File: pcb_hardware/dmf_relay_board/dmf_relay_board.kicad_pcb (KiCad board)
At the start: 2 copper layers, 100 x 96.5 mm, 64 parts, among them J1 HVPS, J2 Relays to Electrodes 1, J3 Relays to Electrodes 2, J4 Electrodes from Relay 1, J5 Electrodes from Relay 2, U1 HV507

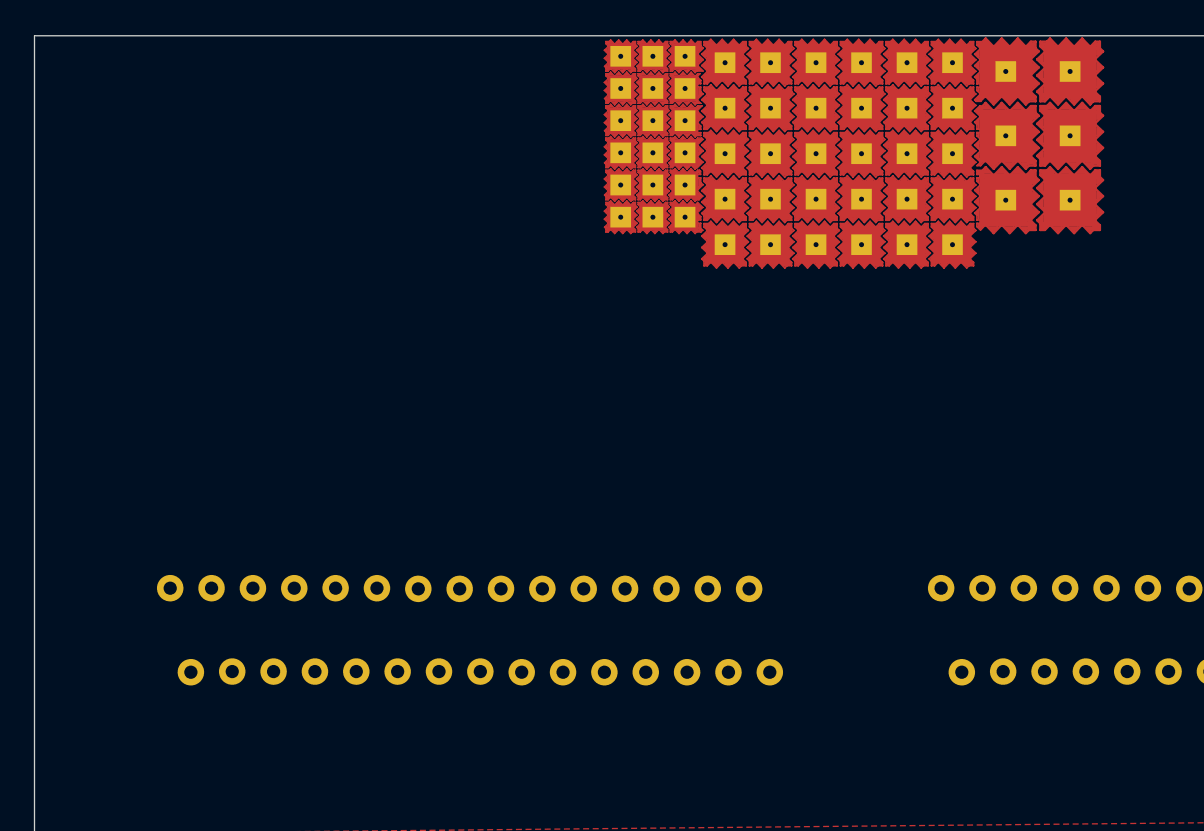
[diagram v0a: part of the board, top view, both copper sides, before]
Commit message: electrode configuration changed for routing management
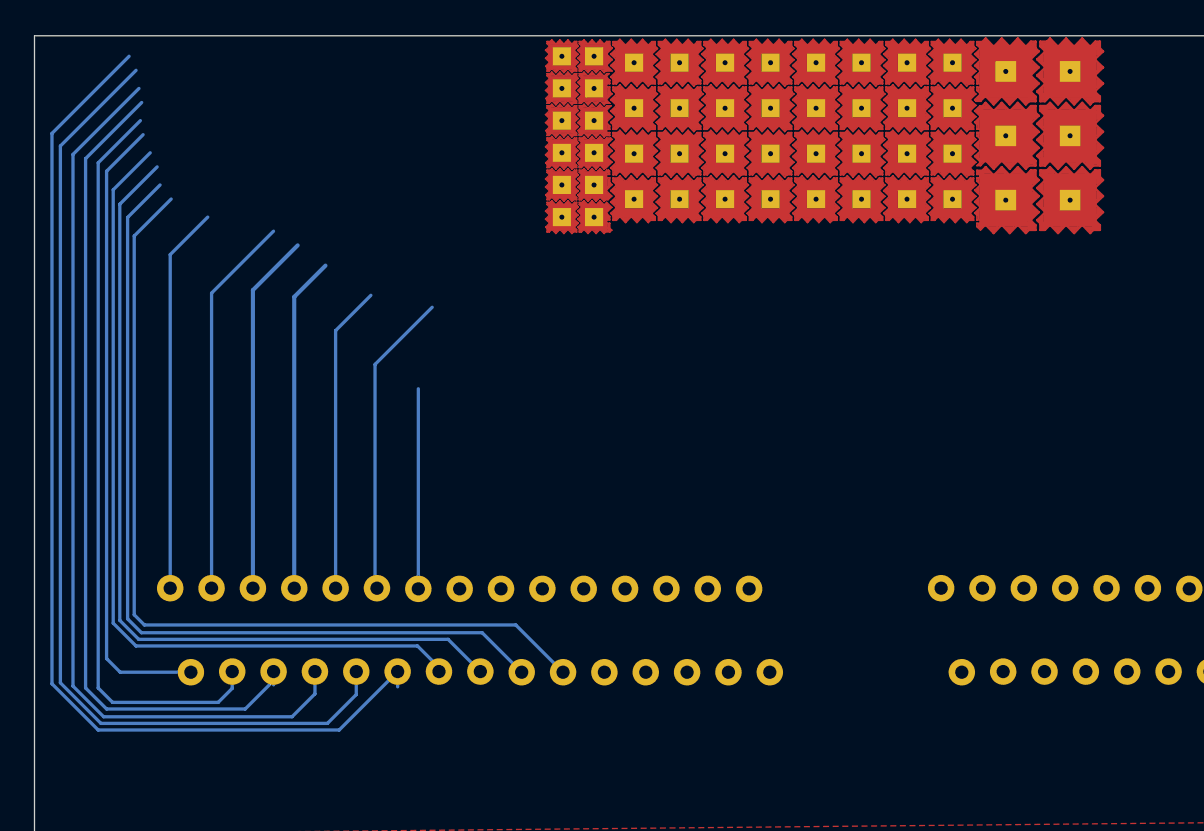
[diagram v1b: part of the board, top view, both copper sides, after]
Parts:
- removed EXS13, EXS14, EXS16, EXS17: ELEC_XS, dmf_relay_board:ELECTRODE_1_375_4MIL_4_5
- removed EXS15: ELEC_XS_TO_SM_5, dmf_relay_board:ELEC_XS_TO_SM_NUM5
- removed EXS18: ELEC_XS_TO_SM_6, dmf_relay_board:ELEC_XS_TO_SM_NUM6
- added ESM31: ELEC_SML, dmf_relay_board:ELECTRODE_2_75_4MIL_4_5, F.Cu at (164.7, 63.9)
- added ESM32: ELEC_SML, dmf_relay_board:ELECTRODE_2_75_4MIL_4_5, F.Cu at (167.5, 63.9)
- EXS10: value ELEC_XS -> ELEC_XS_TO_SM_5; footprint dmf_relay_board:ELECTRODE_1_375_4MIL_4_5 -> dmf_relay_board:ELEC_XS_TO_SM_NUM5
- EXS12: value ELEC_XS_TO_SM_4 -> ELEC_XS_TO_SM_6; footprint dmf_relay_board:ELEC_XS_TO_SM_NUM4 -> dmf_relay_board:ELEC_XS_TO_SM_NUM6
- EXS2: value ELEC_XS -> ELEC_XS_TO_SM_1; footprint dmf_relay_board:ELECTRODE_1_375_4MIL_4_5 -> dmf_relay_board:ELEC_XS_TO_SM_NUM1
- EXS3: value ELEC_XS_TO_SM_1 -> ELEC_XS; footprint dmf_relay_board:ELEC_XS_TO_SM_NUM1 -> dmf_relay_board:ELECTRODE_1_375_4MIL_4_5
- EXS4: value ELEC_XS -> ELEC_XS_TO_SM_2; footprint dmf_relay_board:ELECTRODE_1_375_4MIL_4_5 -> dmf_relay_board:ELEC_XS_TO_SM_NUM2
- EXS6: value ELEC_XS_TO_SM_2 -> ELEC_XS_TO_SM_3; footprint dmf_relay_board:ELEC_XS_TO_SM_NUM2 -> dmf_relay_board:ELEC_XS_TO_SM_NUM3
- EXS8: value ELEC_XS -> ELEC_XS_TO_SM_4; footprint dmf_relay_board:ELECTRODE_1_375_4MIL_4_5 -> dmf_relay_board:ELEC_XS_TO_SM_NUM4
- EXS9: value ELEC_XS_TO_SM_3 -> ELEC_XS; footprint dmf_relay_board:ELEC_XS_TO_SM_NUM3 -> dmf_relay_board:ELECTRODE_1_375_4MIL_4_5
- moved ESM17 16.5 mm to (148.2, 61.2)
- moved ESM18 16.5 mm to (151.0, 61.2)
- moved ESM7 11.3 mm to (164.7, 55.7)
- moved ESM8 11.3 mm to (167.5, 55.7)
- moved ESM10 11.0 mm to (151.0, 58.4)
- moved ESM11 11.0 mm to (153.7, 58.4)
- moved ESM12 11.0 mm to (156.5, 58.4)
- moved ESM9 11.0 mm to (148.2, 58.4)
- moved EXS9 8.40 mm to (143.9, 63.1)
- moved EXS3 7.70 mm to (143.9, 57.2)
- moved EXS11 6.74 mm to (143.9, 65.0)
- moved EXS12 6.74 mm to (145.8, 65.0)
- moved ESM13 6.15 mm to (159.2, 58.4)
- moved ESM14 6.15 mm to (162.0, 58.4)
- moved ESM15 6.15 mm to (164.7, 58.4)
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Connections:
- J4 pad 1: Net-(EXS1-Pad1) -> Net-(J4-Pad1)
- J4 pad 10: Net-(EXS8-Pad1) -> Net-(J4-Pad10)
- J4 pad 11: Net-(EXS9-Pad1) -> Net-(J4-Pad11)
- J4 pad 13: Net-(EXS10-Pad1) -> Net-(J4-Pad13)
- J4 pad 14: Net-(EXS11-Pad1) -> Net-(J4-Pad14)
- J4 pad 15: Net-(EXS12-Pad1) -> Net-(J4-Pad15)
- J4 pad 2: Net-(EXS2-Pad1) -> Net-(J4-Pad2)
- J4 pad 22: Net-(ELG6-Pad1) -> Net-(J4-Pad22)
- J4 pad 24: Net-(ELG5-Pad1) -> Net-(J4-Pad24)
- J4 pad 26: Net-(ESM30-Pad1) -> Net-(J4-Pad26)
- J4 pad 28: Net-(ESM29-Pad1) -> Net-(J4-Pad28)
- J4 pad 3: Net-(EXS3-Pad1) -> Net-(J4-Pad3)
- J4 pad 30: Net-(ESM28-Pad1) -> Net-(J4-Pad30)
- J4 pad 5: Net-(EXS4-Pad1) -> Net-(J4-Pad5)
- J4 pad 6: Net-(EXS5-Pad1) -> Net-(J4-Pad6)
- J4 pad 7: Net-(EXS6-Pad1) -> Net-(J4-Pad7)
- J4 pad 9: Net-(EXS7-Pad1) -> Net-(J4-Pad9)
- J5 pad 11: Net-(J5-Pad11) -> Net-(EXS10-Pad1)
- J5 pad 13: Net-(J5-Pad13) -> Net-(EXS9-Pad1)
- J5 pad 14: Net-(EXS16-Pad1) -> Net-(ESM13-Pad1)
- J5 pad 15: Net-(J5-Pad15) -> Net-(EXS8-Pad1)
- J5 pad 16: Net-(J5-Pad16) -> Net-(ESM19-Pad1)
- J5 pad 17: Net-(J5-Pad17) -> Net-(EXS7-Pad1)
- J5 pad 18: Net-(J5-Pad18) -> Net-(ESM25-Pad1)
- J5 pad 19: Net-(J5-Pad19) -> Net-(EXS1-Pad1)
- J5 pad 20: Net-(ESM14-Pad1) -> Net-(ESM7-Pad1)
- J5 pad 21: Net-(J5-Pad21) -> Net-(EXS2-Pad1)
- J5 pad 22: Net-(J5-Pad22) -> Net-(ESM1-Pad1)
- J5 pad 23: Net-(J5-Pad23) -> Net-(EXS3-Pad1)
- J5 pad 25: Net-(J5-Pad25) -> Net-(EXS4-Pad1)
- J5 pad 27: Net-(J5-Pad27) -> Net-(EXS5-Pad1)
- J5 pad 28: Net-(J5-Pad28) -> Net-(EXS12-Pad1)
- J5 pad 29: Net-(J5-Pad29) -> Net-(EXS6-Pad1)
- J5 pad 30: Net-(J5-Pad30) -> Net-(EXS11-Pad1)
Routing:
- net Net-(EXS1-Pad1): track 0.00 -> 64.4 mm
- net Net-(EXS2-Pad1): track 0.00 -> 61.1 mm
- net Net-(EXS3-Pad1): track 0.00 -> 55.1 mm
- net Net-(EXS10-Pad1): track 0.00 -> 54.6 mm
- net Net-(EXS8-Pad1): track 0.00 -> 52.6 mm
- net Net-(EXS9-Pad1): track 0.00 -> 52.2 mm
- net Net-(EXS4-Pad1): track 0.00 -> 52.0 mm
- net Net-(EXS7-Pad1): track 0.00 -> 50.4 mm
- net Net-(EXS5-Pad1): track 0.00 -> 45.2 mm
- net Net-(EXS6-Pad1): track 0.00 -> 39.2 mm
- net Net-(EXS12-Pad1): track 0.00 -> 24.4 mm
- net Net-(EXS11-Pad1): track 0.00 -> 23.6 mm
- net Net-(J5-Pad26): track 0.00 -> 22.1 mm
- net Net-(J5-Pad24): track 0.00 -> 20.4 mm
- net Net-(ESM1-Pad1): track 0.00 -> 18.6 mm
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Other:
- net class ELEC_HV: clearance 0 -> 0.2

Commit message: gerbers created, routes cmplt
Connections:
- J4 pad 1: Net-(J4-Pad1) -> Net-(ELG1-Pad1)
- J4 pad 10: Net-(J4-Pad10) -> Net-(ESM8-Pad1)
- J4 pad 12: Net-(J4-Pad12) -> Net-(ESM23-Pad1)
- J4 pad 14: Net-(J4-Pad14) -> Net-(ESM31-Pad1)
- J4 pad 16: Net-(J4-Pad16) -> Net-(ESM15-Pad1)
- J4 pad 18: Net-(J4-Pad18) -> Net-(ESM7-Pad1)
- J4 pad 2: Net-(J4-Pad2) -> Net-(ELG5-Pad1)
- J4 pad 20: Net-(J4-Pad20) -> Net-(ESM22-Pad1)
- J4 pad 21: Net-(J4-Pad21) -> Net-(ESM13-Pad1)
- J4 pad 22: Net-(J4-Pad22) -> Net-(ESM30-Pad1)
- J4 pad 23: Net-(J4-Pad23) -> Net-(ESM5-Pad1)
- J4 pad 24: Net-(J4-Pad24) -> Net-(ESM14-Pad1)
- J4 pad 25: Net-(J4-Pad25) -> Net-(ESM20-Pad1)
- J4 pad 26: Net-(J4-Pad26) -> Net-(ESM6-Pad1)
- J4 pad 27: Net-(J4-Pad27) -> Net-(ESM28-Pad1)
- J4 pad 28: Net-(J4-Pad28) -> Net-(ESM21-Pad1)
- J4 pad 29: Net-(J4-Pad29) -> Net-(ESM12-Pad1)
- J4 pad 3: Net-(J4-Pad3) -> Net-(ELG2-Pad1)
- J4 pad 30: Net-(J4-Pad30) -> Net-(ESM29-Pad1)
- J4 pad 4: Net-(J4-Pad4) -> Net-(ESM24-Pad1)
- J4 pad 5: Net-(J4-Pad5) -> Net-(ELG3-Pad1)
- J4 pad 6: Net-(J4-Pad6) -> Net-(ESM32-Pad1)
- J4 pad 7: Net-(J4-Pad7) -> Net-(ELG4-Pad1)
- J4 pad 8: Net-(J4-Pad8) -> Net-(ESM16-Pad1)
- J4 pad 9: Net-(J4-Pad9) -> Net-(ELG6-Pad1)
- J5 pad 10: Net-(J5-Pad10) -> Net-(ESM3-Pad1)
- J5 pad 12: Net-(J5-Pad12) -> Net-(ESM18-Pad1)
- J5 pad 14: Net-(ESM13-Pad1) -> Net-(ESM26-Pad1)
- J5 pad 16: Net-(ESM19-Pad1) -> Net-(ESM10-Pad1)
- J5 pad 18: Net-(ESM25-Pad1) -> Net-(ESM2-Pad1)
- J5 pad 2: Net-(J5-Pad2) -> Net-(ESM4-Pad1)
- J5 pad 20: Net-(ESM7-Pad1) -> Net-(ESM17-Pad1)
- J5 pad 22: Net-(ESM1-Pad1) -> Net-(ESM25-Pad1)
- J5 pad 24: Net-(J5-Pad24) -> Net-(ESM9-Pad1)
- J5 pad 26: Net-(J5-Pad26) -> Net-(ESM1-Pad1)
- J5 pad 4: Net-(J5-Pad4) -> Net-(ESM19-Pad1)
- J5 pad 6: Net-(J5-Pad6) -> Net-(ESM27-Pad1)
- J5 pad 8: Net-(J5-Pad8) -> Net-(ESM11-Pad1)
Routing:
- net Net-(ELG1-Pad1): track 0.00 -> 74.3 mm
- net Net-(ELG3-Pad1): track 0.00 -> 72.9 mm
- net Net-(ELG2-Pad1): track 0.00 -> 69.4 mm
- net Net-(ELG4-Pad1): track 0.00 -> 67.3 mm
- net Net-(ELG6-Pad1): track 0.00 -> 64.9 mm, vias 0 -> 1
- net Net-(ESM5-Pad1): track 0.00 -> 49.7 mm, vias 0 -> 1
- net Net-(ESM8-Pad1): track 0.00 -> 48.7 mm
- net Net-(ESM13-Pad1): track 0.00 -> 48.1 mm, vias 0 -> 1
- net Net-(ESM24-Pad1): track 0.00 -> 48.0 mm
- net Net-(ESM16-Pad1): track 0.00 -> 47.6 mm
- net Net-(ELG5-Pad1): track 0.00 -> 45.7 mm
- net Net-(ESM9-Pad1): track 0.00 -> 44.4 mm
- net Net-(ESM32-Pad1): track 0.00 -> 43.3 mm
- net Net-(ESM2-Pad1): track 0.00 -> 41.5 mm
- net Net-(ESM12-Pad1): track 0.00 -> 41.3 mm
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
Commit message: preparing change to 4 layer to meet IPC2221
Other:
- copper layers 2 -> 4

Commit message: 4 layer board cmplt
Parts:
- removed the EXS3 at (143.9, 57.2)
- removed the EXS9 at (143.9, 63.1)
- added ESM33: ELEC_SML, dmf_relay_board:ELECTRODE_2_75_4MIL_4_5, F.Cu at (160.6, 69.2)
- added ESM34: ELEC_SML, dmf_relay_board:ELECTRODE_2_75_4MIL_4_5, F.Cu at (163.3, 69.2)
- added ESM35: ELEC_SML, dmf_relay_board:ELECTRODE_2_75_4MIL_4_5, F.Cu at (166.1, 69.2)
- added ESM36: ELEC_SML, dmf_relay_board:ELECTRODE_2_75_4MIL_4_5, F.Cu at (168.8, 69.2)
- added EXS10: ELEC_XS, dmf_relay_board:ELECTRODE_1_375_4MIL_4_5, F.Cu at (148.8, 60.9)
- added EXS13: ELEC_XS, dmf_relay_board:ELECTRODE_1_375_4MIL_4_5, F.Cu at (148.8, 62.8)
- added EXS14: ELEC_XS, dmf_relay_board:ELECTRODE_1_375_4MIL_4_5, F.Cu at (150.7, 62.8)
- added EXS16: ELEC_XS, dmf_relay_board:ELECTRODE_1_375_4MIL_4_5, F.Cu at (148.8, 64.8)
- added EXS17: ELEC_XS, dmf_relay_board:ELECTRODE_1_375_4MIL_4_5, F.Cu at (150.7, 64.8)
- added EXS2: ELEC_XS, dmf_relay_board:ELECTRODE_1_375_4MIL_4_5, F.Cu at (150.7, 55.0)
- added EXS4: ELEC_XS, dmf_relay_board:ELECTRODE_1_375_4MIL_4_5, F.Cu at (148.8, 57.0)
- added EXS8: ELEC_XS, dmf_relay_board:ELECTRODE_1_375_4MIL_4_5, F.Cu at (150.7, 58.9)
- added M1: MountingHole_3.2mm_M3, MountingHole:MountingHole_3.2mm_M3, F.Cu at (118.0, 60.0)
- added M2: MountingHole_3.2mm_M3, MountingHole:MountingHole_3.2mm_M3, F.Cu at (206.0, 60.0)
- added M3: MountingHole_3.2mm_M3, MountingHole:MountingHole_3.2mm_M3, F.Cu at (118.0, 138.5)
- added M4: MountingHole_3.2mm_M3, MountingHole:MountingHole_3.2mm_M3, F.Cu at (206.0, 144.5)
- moved ESM17 17.9 mm to (166.1, 60.9)
- moved ESM18 17.9 mm to (168.8, 60.9)
- moved ESM10 12.4 mm to (163.3, 58.2)
- moved ESM11 12.4 mm to (166.1, 58.2)
- moved ESM12 12.4 mm to (168.8, 58.2)
- moved ESM9 12.4 mm to (160.6, 58.2)
- moved ESM31 11.0 mm to (155.1, 69.2)
- moved ESM32 11.0 mm to (157.8, 69.2)
- moved ESM7 9.94 mm to (155.1, 58.2)
- moved ESM8 9.94 mm to (157.8, 58.2)
- moved EXS11 8.03 mm to (150.7, 60.9)
- moved ESM25 7.31 mm to (155.1, 66.4)
- moved ESM26 7.31 mm to (157.8, 66.4)
- moved ESM27 7.31 mm to (160.6, 66.4)
- moved ESM28 7.31 mm to (163.3, 66.4)
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- renumbered EXS8 to EXS12, EXS10 to EXS15, EXS12 to EXS18, EXS2 to EXS3, EXS4 to EXS6, EXS6 to EXS9
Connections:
- EXS12 pad 1: Net-(EXS8-Pad1) -> Net-(EXS12-Pad1)
- EXS15 pad 1: Net-(EXS10-Pad1) -> Net-(EXS15-Pad1)
- EXS18 pad 1: Net-(EXS12-Pad1) -> Net-(EXS18-Pad1)
- EXS3 pad 1: Net-(EXS2-Pad1) -> Net-(EXS3-Pad1)
- EXS6 pad 1: Net-(EXS4-Pad1) (its old number) -> Net-(EXS6-Pad1)
- EXS9 pad 1: Net-(EXS6-Pad1) -> Net-(EXS9-Pad1)
- J4 pad 1: Net-(ELG1-Pad1) -> Net-(ELG2-Pad1)
- J4 pad 10: Net-(ESM8-Pad1) -> Net-(ESM12-Pad1)
- J4 pad 11: Net-(J4-Pad11) -> Net-(ELG5-Pad1)
- J4 pad 12: Net-(ESM23-Pad1) -> Net-(ESM6-Pad1)
- J4 pad 13: Net-(J4-Pad13) -> Net-(ESM3-Pad1)
- J4 pad 14: Net-(ESM31-Pad1) -> Net-(ESM29-Pad1)
- J4 pad 15: Net-(J4-Pad15) -> Net-(ESM9-Pad1)
- J4 pad 16: Net-(ESM15-Pad1) -> Net-(ESM35-Pad1)
- J4 pad 17: Net-(J4-Pad17) -> Net-(ESM15-Pad1)
- J4 pad 18: Net-(ESM7-Pad1) -> Net-(ESM23-Pad1)
- J4 pad 19: Net-(J4-Pad19) -> Net-(ESM21-Pad1)
- J4 pad 2: Net-(ELG5-Pad1) -> Net-(ESM30-Pad1)
- J4 pad 20: Net-(ESM22-Pad1) -> Net-(ESM17-Pad1)
- J4 pad 21: Net-(ESM13-Pad1) -> Net-(ESM27-Pad1)
- J4 pad 22: Net-(ESM30-Pad1) -> Net-(ESM11-Pad1)
- J4 pad 23: Net-(ESM5-Pad1) -> Net-(ESM33-Pad1)
- J4 pad 24: Net-(ESM14-Pad1) -> Net-(ESM5-Pad1)
- J4 pad 25: Net-(ESM20-Pad1) -> Net-(ESM16-Pad1)
- J4 pad 26: Net-(ESM6-Pad1) -> Net-(ESM28-Pad1)
- J4 pad 27: Net-(ESM28-Pad1) -> Net-(ESM10-Pad1)
- J4 pad 28: Net-(ESM21-Pad1) -> Net-(ESM34-Pad1)
- J4 pad 29: Net-(ESM12-Pad1) -> Net-(ESM4-Pad1)
- J4 pad 3: Net-(ELG2-Pad1) -> Net-(ELG1-Pad1)
- J4 pad 30: Net-(ESM29-Pad1) -> Net-(ESM22-Pad1)
- J4 pad 4: Net-(ESM24-Pad1) -> Net-(ESM36-Pad1)
- J4 pad 5: Net-(ELG3-Pad1) -> Net-(ELG4-Pad1)
- J4 pad 6: Net-(ESM32-Pad1) -> Net-(ESM24-Pad1)
- J4 pad 7: Net-(ELG4-Pad1) -> Net-(ELG3-Pad1)
- J4 pad 8: Net-(ESM16-Pad1) -> Net-(ESM18-Pad1)
- J5 pad 1: Net-(J5-Pad1) -> Net-(ESM32-Pad1)
- J5 pad 10: Net-(ESM3-Pad1) -> Net-(ESM7-Pad1)
- J5 pad 11: Net-(EXS10-Pad1) -> Net-(ESM2-Pad1)
- J5 pad 12: Net-(ESM18-Pad1) -> Net-(ESM1-Pad1)
- J5 pad 13: Net-(EXS9-Pad1) -> Net-(EXS3-Pad1)
- J5 pad 14: Net-(ESM26-Pad1) -> Net-(EXS16-Pad1)
- J5 pad 15: Net-(EXS8-Pad1) -> Net-(EXS2-Pad1)
- J5 pad 16: Net-(ESM10-Pad1) -> Net-(EXS17-Pad1)
- J5 pad 17: Net-(EXS7-Pad1) -> Net-(EXS1-Pad1)
- J5 pad 18: Net-(ESM2-Pad1) -> Net-(EXS18-Pad1)
- J5 pad 19: Net-(EXS1-Pad1) -> Net-(EXS6-Pad1)
- J5 pad 2: Net-(ESM4-Pad1) -> Net-(ESM31-Pad1)
- J5 pad 20: Net-(ESM17-Pad1) -> Net-(EXS13-Pad1)
- J5 pad 21: Net-(EXS2-Pad1) -> Net-(EXS5-Pad1)
- J5 pad 22: Net-(ESM25-Pad1) -> Net-(EXS14-Pad1)
- J5 pad 24: Net-(ESM9-Pad1) -> Net-(EXS15-Pad1)
- J5 pad 25: Net-(EXS4-Pad1) (its old number) -> Net-(EXS9-Pad1)
- J5 pad 26: Net-(ESM1-Pad1) -> Net-(EXS10-Pad1)
- J5 pad 27: Net-(EXS5-Pad1) -> Net-(EXS8-Pad1)
- J5 pad 28: Net-(EXS12-Pad1) -> Net-(EXS11-Pad1)
- J5 pad 29: Net-(EXS6-Pad1) -> Net-(EXS7-Pad1)
- J5 pad 3: Net-(J5-Pad3) -> Net-(ESM26-Pad1)
- J5 pad 30: Net-(EXS11-Pad1) -> Net-(EXS12-Pad1)
- J5 pad 4: Net-(ESM19-Pad1) -> Net-(ESM25-Pad1)
- J5 pad 5: Net-(J5-Pad5) -> Net-(ESM20-Pad1)
- J5 pad 6: Net-(ESM27-Pad1) -> Net-(ESM19-Pad1)
- J5 pad 7: Net-(J5-Pad7) -> Net-(ESM14-Pad1)
- J5 pad 8: Net-(ESM11-Pad1) -> Net-(ESM13-Pad1)
- J5 pad 9: Net-(J5-Pad9) -> Net-(ESM8-Pad1)
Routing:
- net Net-(EXS3-Pad1): track 0.00 -> 97.9 mm
- net Net-(EXS4-Pad1) (its old number): track 78.5 -> 0.00 mm
- net Net-(EXS15-Pad1): track 0.00 -> 46.5 mm
- net Net-(ESM36-Pad1): track 0.00 -> 43.3 mm
- net Net-(EXS14-Pad1): track 0.00 -> 41.9 mm
- net Net-(ESM33-Pad1): track 0.00 -> 38.4 mm
- net Net-(EXS18-Pad1): track 0.00 -> 37.8 mm
- net Net-(EXS13-Pad1): track 0.00 -> 37.4 mm
- net Net-(ESM3-Pad1): track 35.3 -> 70.1 mm
- net Net-(EXS17-Pad1): track 0.00 -> 33.2 mm
- net Net-(EXS10-Pad1): track 79.3 -> 47.1 mm
- net Net-(ESM35-Pad1): track 0.00 -> 31.7 mm
- net Net-(EXS16-Pad1): track 0.00 -> 29.5 mm
- net Net-(ESM34-Pad1): track 0.00 -> 24.3 mm
- net CHNL_55: track 58.5 -> 82.7 mm, vias 1 -> 0
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- added copper zone on In2.Cu, net GND
- added copper zone on In1.Cu, net VPP
- removed copper zone on F.Cu, net GND
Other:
- net class DMF_HV: clearance 0.25 -> 0.2
- net class ELEC_HV removed
- net class ELEC_HV_EXT added: clearance 0.2, trace_width 0.2, via_dia 0.6, via_drill 0.3
- net class ELEC_HV_INT added: clearance 0.2, trace_width 0.2, via_dia 0.6, via_drill 0.3

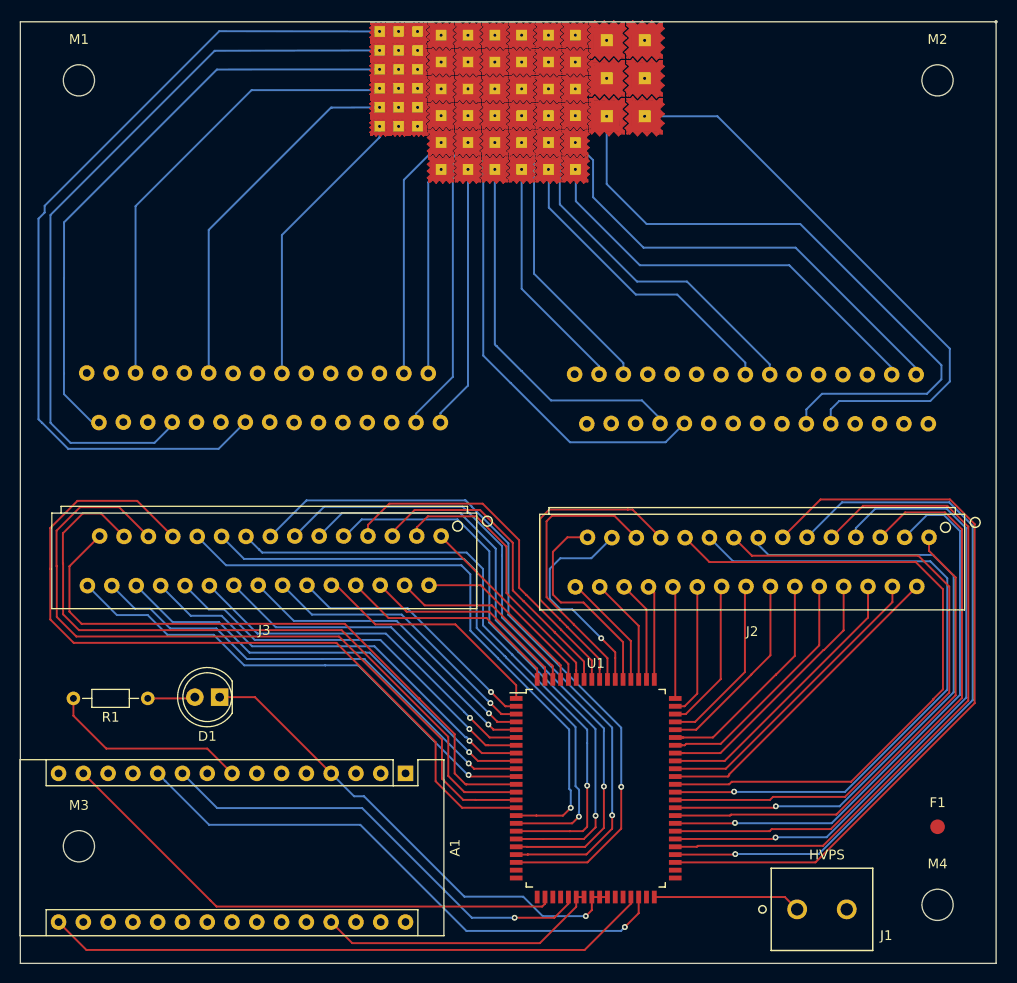
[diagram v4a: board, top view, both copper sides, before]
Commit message: pcb mounting holes adjusted
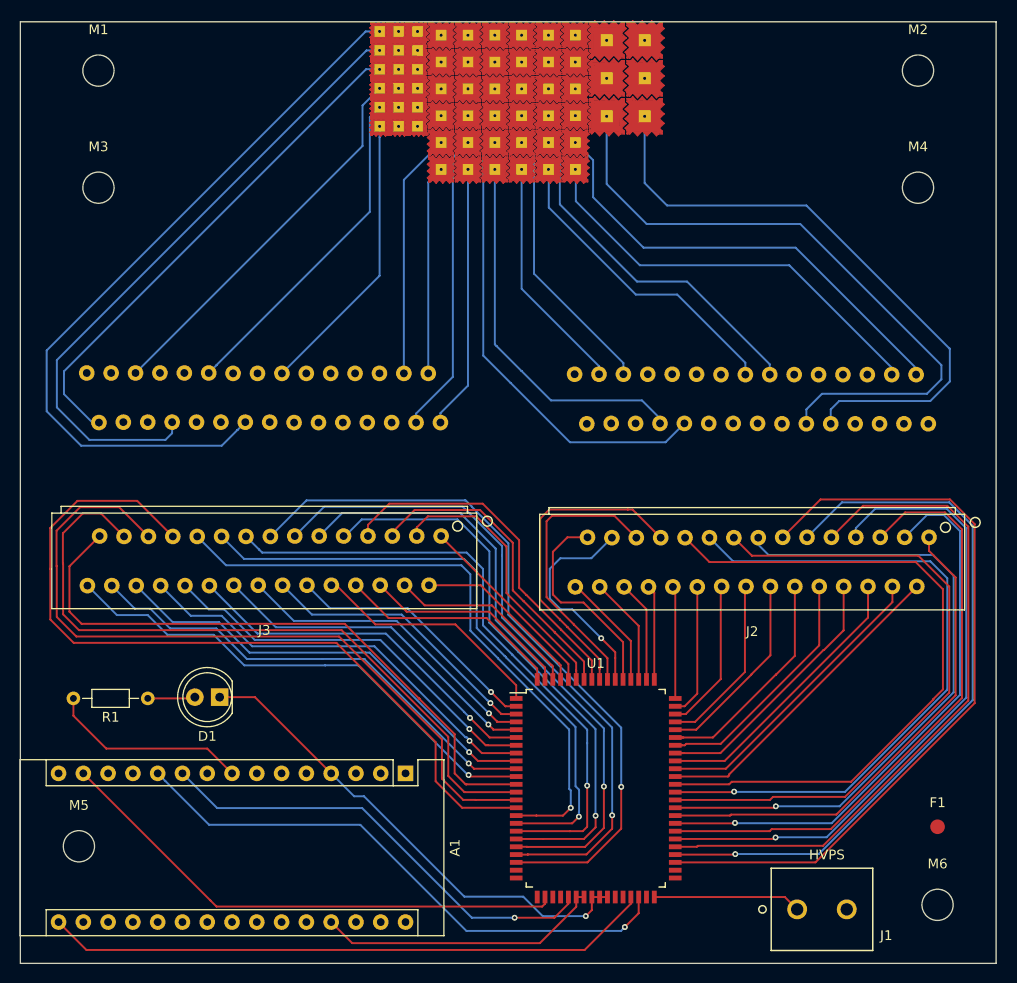
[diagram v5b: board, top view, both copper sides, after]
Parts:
- added M3: MountingHole_3.2mm_M3, MountingHole:MountingHole_3.2mm_M3, F.Cu at (120.0, 71.0)
- added M4: MountingHole_3.2mm_M3, MountingHole:MountingHole_3.2mm_M3, F.Cu at (204.0, 71.0)
- moved M1 2.24 mm to (120.0, 59.0)
- moved M2 2.24 mm to (204.0, 59.0)
- renumbered M3 to M5, M4 to M6
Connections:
- J4 pad 3: Net-(ELG1-Pad1) -> Net-(ELG4-Pad1)
- J4 pad 5: Net-(ELG4-Pad1) -> Net-(ELG1-Pad1)
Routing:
- net Net-(EXS5-Pad1): track 82.4 -> 71.0 mm
- net Net-(EXS6-Pad1): track 87.1 -> 75.7 mm
- net Net-(EXS1-Pad1): track 87.5 -> 76.7 mm
- net Net-(EXS4-Pad1): track 77.0 -> 66.6 mm
- net Net-(EXS2-Pad1): track 92.8 -> 82.5 mm
- net Net-(EXS12-Pad1): track 56.2 -> 46.0 mm
- net Net-(EXS3-Pad1): track 97.9 -> 87.9 mm
- net Net-(EXS8-Pad1): track 65.9 -> 56.6 mm
- net Net-(EXS11-Pad1): track 51.6 -> 42.4 mm
- net Net-(EXS7-Pad1): track 61.2 -> 52.3 mm
- net Net-(EXS9-Pad1): track 71.5 -> 62.7 mm
- net Net-(EXS10-Pad1): track 47.1 -> 39.8 mm
- net Net-(EXS15-Pad1): track 46.5 -> 39.9 mm
- net Net-(ELG1-Pad1): track 61.1 -> 66.8 mm
- net Net-(EXS14-Pad1): track 41.9 -> 36.3 mm
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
